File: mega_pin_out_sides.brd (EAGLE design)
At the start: 100 x 85 mm, 101 parts, among them T1 2N2222, T10 2N2222, T11 2N2222, T12 2N2222, T13 2N2222, T14 2N2222, T15 2N2222, T16 2N2222, T17 2N2222, T18 2N2222, T2 2N2222, T3 2N2222, T4 2N2222, T5 2N2222, T6 2N2222, T7 2N2222, T8 2N2222, T9 2N2222

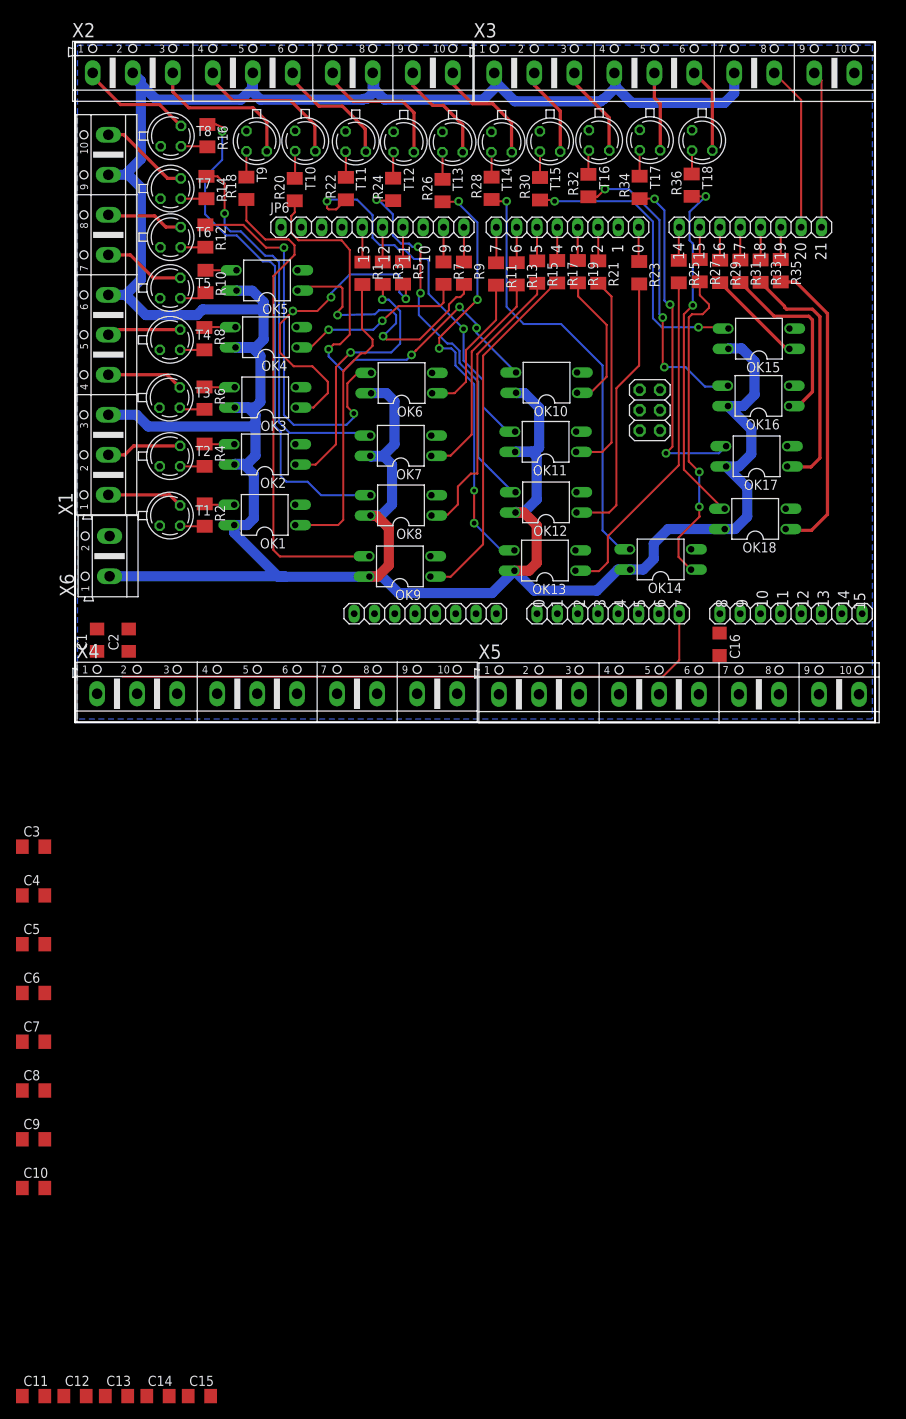
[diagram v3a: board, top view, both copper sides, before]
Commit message: [SIDES] Fix major issue where GND was common
- Fix a major bug in the design where the Vext GND and Arduino GND were common. They have been isolated correctly.
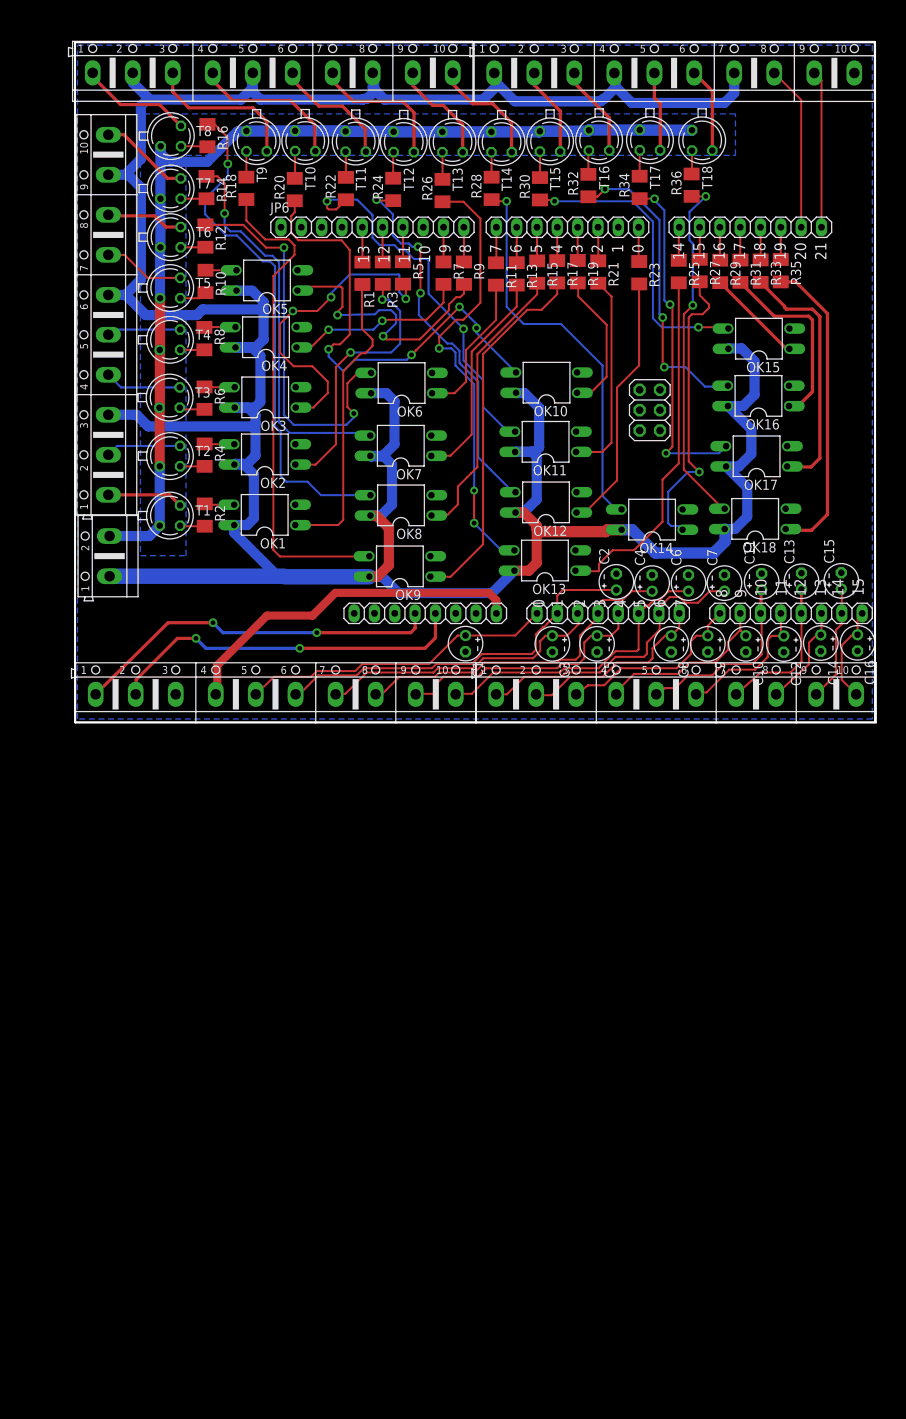
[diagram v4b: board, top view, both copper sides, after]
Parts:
- C1, C10, C11, C12, C13, C14, C15, C16, C2, C3, C4, C5, C6, C7, C8, C9: device resistor:C1206 -> adafruit:E2-4
- moved C11 136.6 mm to (85.8, 17.6), turned to 90 degrees
- moved C13 133.1 mm to (90.8, 17.6), turned to 90 degrees
- moved C15 129.7 mm to (95.8, 17.7), turned to 90 degrees
- moved C12 129.2 mm to (88.6, 9.78), turned to 270 degrees
- moved C14 125.4 mm to (93.2, 9.91), turned to 270 degrees
- moved C10 112.0 mm to (83.8, 9.80), turned to 270 degrees
- moved C9 104.6 mm to (79.1, 9.80), turned to 270 degrees
- moved C7 103.7 mm to (81.2, 17.4), turned to 90 degrees
- moved C8 97.3 mm to (74.5, 9.80), turned to 270 degrees
- moved C6 96.6 mm to (76.7, 17.4), turned to 90 degrees
- moved C4 86.6 mm to (72.1, 17.4), turned to 90 degrees
- moved C5 79.8 mm to (65.3, 9.80), turned to 270 degrees
- moved C3 69.6 mm to (59.7, 9.80), turned to 270 degrees
- moved C2 61.4 mm to (67.7, 17.6)
- moved C1 46.1 mm to (48.8, 9.83), turned to 270 degrees
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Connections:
- new net GNDEXT: T1.1, T10.1, T11.1, T12.1, T13.1, T14.1, T15.1, T16.1, T17.1, T18.1, T2.1, T3.1, T4.1, T5.1, T6.1, T7.1, T8.1, T9.1, X6.2
- net A0: now also ADCL.1, C1.+; no longer ADCL.8
- net A1: now also ADCL.2, C2.+; no longer ADCL.7
- net A10: now also ADCH.3, C11.+; no longer ADCH.6, C11.1
- net A11: now also ADCH.4, C12.+; no longer ADCH.5, C12.1
- net A12: now also ADCH.5, C13.+; no longer ADCH.4, C13.1
- net A13: now also ADCH.6, C14.+; no longer ADCH.3, C14.1
- net A14: now also ADCH.7, C15.+; no longer ADCH.2, C15.1
- net A15: now also ADCH.8, C16.+; no longer ADCH.1, C16.1
- net A2: now also ADCL.3, C3.+; no longer ADCL.6
- net A3: now also ADCL.4, C4.+; no longer ADCL.5
- net A4: now also ADCL.5, C5.+; no longer ADCL.4
- net A5: now also ADCL.6, C6.+; no longer ADCL.3
- net A6: now also ADCL.7, C7.+; no longer ADCL.2
- net A7: now also ADCL.8, C8.+; no longer ADCL.1
- net A8: now also ADCH.1, C9.+; no longer ADCH.8
- net A9: now also ADCH.2, C10.+; no longer ADCH.7
- net GND: now also C1.-, C10.-, C11.-, C12.-, C13.-, C14.-, C15.-, C16.-, C2.-, C3.-, C4.-, C5.-, C6.-, C7.-, C8.-, C9.-; no longer C1.2, C10.2, C11.2, C12.2, C13.2, C14.2, C15.2, C16.2, C2.2, C3.2, C4.2, C5.2, C6.2, C7.2, C8.2, C9.2, T1.1, T10.1, T11.1, T12.1, T13.1, T14.1, T15.1, T16.1, T17.1, T18.1, T2.1, T3.1, T4.1, T5.1, T6.1, T7.1, T8.1, T9.1
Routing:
- net GNDEXT: track 0.00 -> 124.4 mm
- net A1: track 0.00 -> 48.0 mm
- net 3V3: track 0.00 -> 46.2 mm, vias 0 -> 2
- net 5V: track 0.00 -> 45.5 mm, vias 0 -> 2
- net VIN: track 0.00 -> 44.4 mm
- net A3: track 0.00 -> 42.4 mm
- net A6: track 0.00 -> 37.1 mm
- net A5: track 0.00 -> 37.1 mm
- net A0: track 76.3 -> 39.3 mm
- net A2: track 0.00 -> 36.1 mm
- net A4: track 0.00 -> 32.3 mm
- net A10: track 0.00 -> 26.2 mm
- net A7: track 0.00 -> 23.9 mm
- net A8: track 0.00 -> 23.7 mm
- net A9: track 0.00 -> 22.6 mm
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- added copper zone on layer 16, net N$3

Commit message: [SIDES] Fix DRC Errors
- Fixed all DRC Errors which were related to silk screens mainly.
- Re routed some pins for a better path.
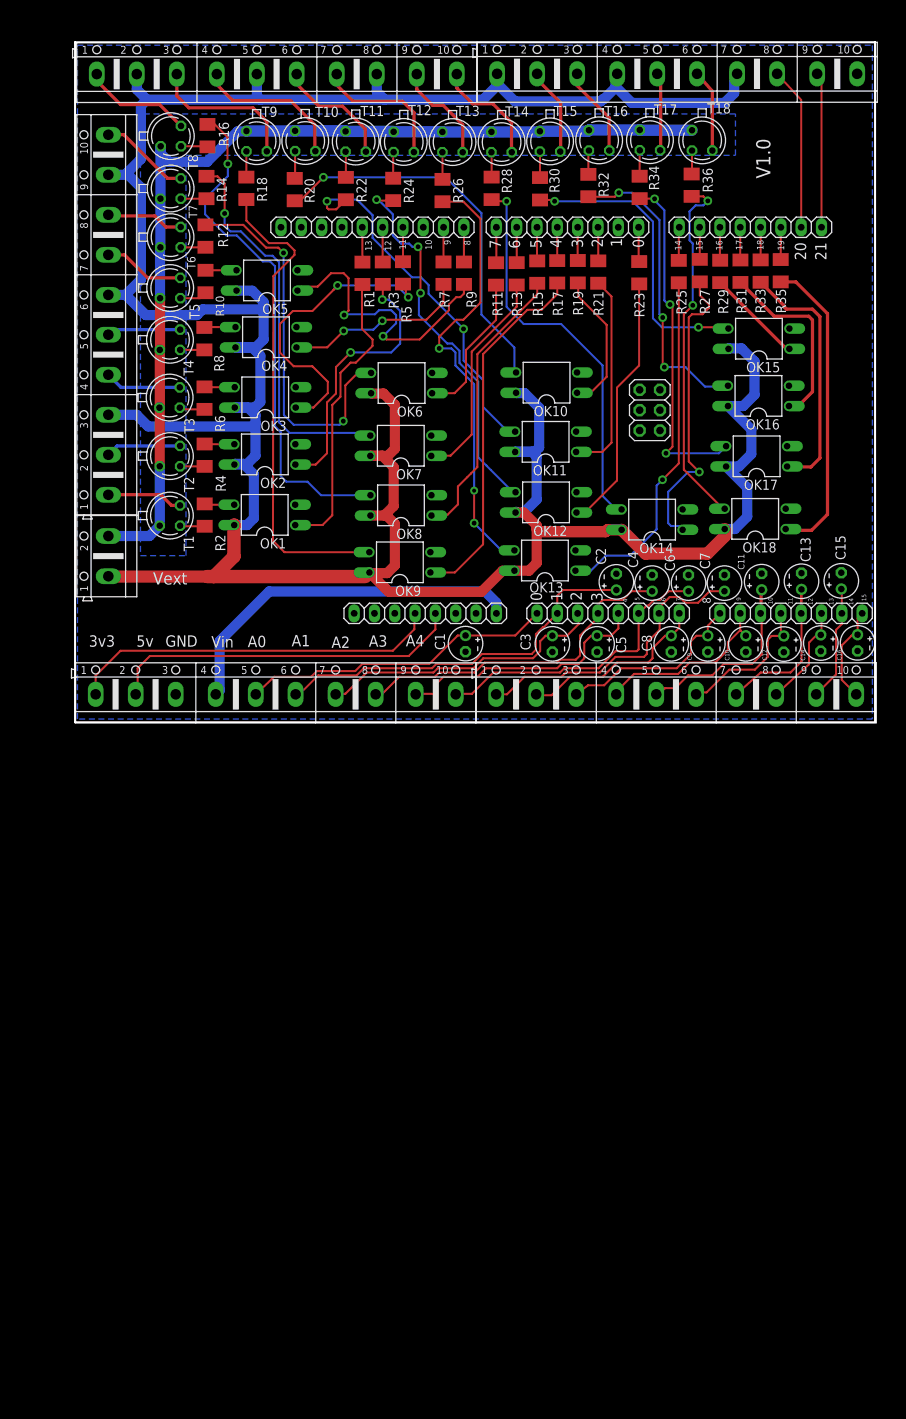
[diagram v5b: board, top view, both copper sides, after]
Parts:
- moved X2 0.53 mm to (25.2, 81.0)
- moved OK9 0.51 mm to (40.6, 20.0)
- moved X3 0.37 mm to (75.3, 81.1)
- moved X6 0.15 mm to (4.16, 20.8)
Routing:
- net N$36: track 58.9 -> 48.1 mm, vias 4 -> 1
- net VEXT: track 407.9 -> 403.4 mm
- net N$8: track 40.4 -> 37.8 mm, vias 3 -> 2
- net N$14: track 34.8 -> 36.9 mm
- net N$39: track 47.8 -> 46.0 mm
- net N$24: track 49.7 -> 48.0 mm
- net VIN: track 44.4 -> 45.9 mm
- net N$33: track 61.5 -> 60.2 mm
- net N$1: track 38.1 -> 37.0 mm
- net 5V: track 45.5 -> 44.6 mm, vias 2 -> 0
- net N$57: track 44.5 -> 45.1 mm
- net N$47: track 44.7 -> 44.3 mm, vias 0 -> 1
- net 3V3: track 46.2 -> 46.6 mm, vias 2 -> 0
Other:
- board text added: "3v3"
- board text added: "5v"
- board text added: "A0"
- board text added: "A1"
- board text added: "A2"
- board text added: "A3"
- board text added: "A4"
- board text added: "GND"
- board text added: "V1.0"
- board text added: "Vext"
- board text added: "Vin"

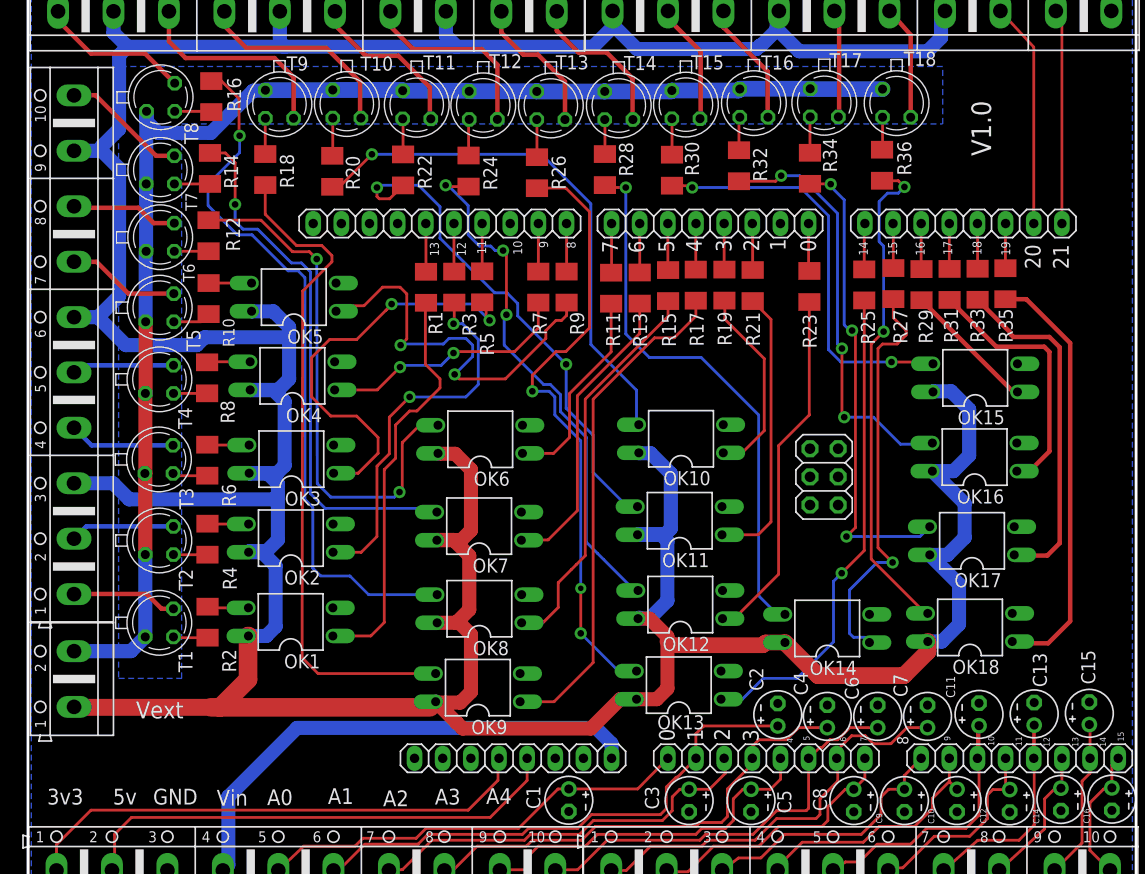
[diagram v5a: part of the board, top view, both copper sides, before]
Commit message: [SIDES] Added header jumper pins for Flashing
- During Flashing or Reset Pin 13, 9 & 0 flashes several times and this will trigger the relays. A header jumper to be removed during flashing and after start up they are back again in place.
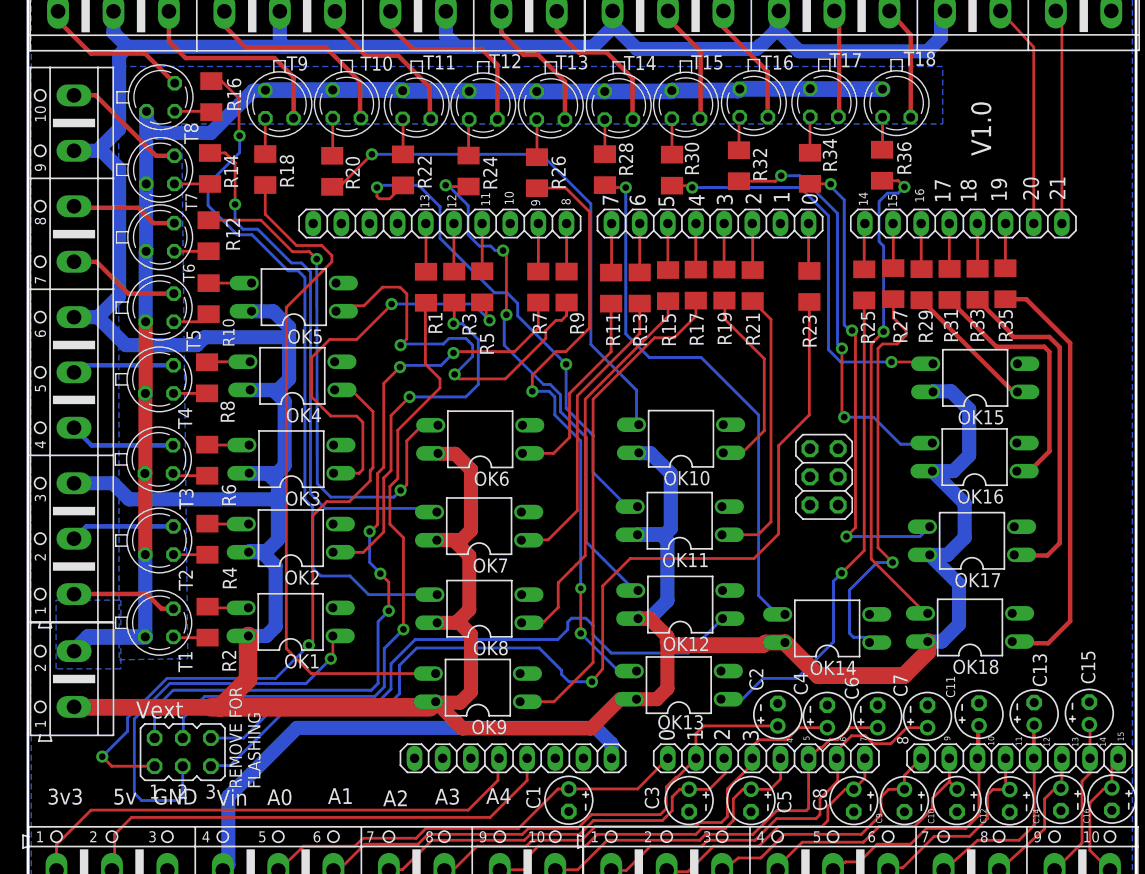
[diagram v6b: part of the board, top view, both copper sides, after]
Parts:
- added JP1: (no value), jumper:JP3Q
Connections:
- new net N$10: JP1.6, OK12.1
- new net N$11: JP1.1, OK4.1
- new net N$9: JP1.3, OK1.1
- net GND: now also X3.10
- net N$1: now also JP1.4; no longer OK1.1
- net N$19: now also JP1.2; no longer OK4.1
- net N$44: now also JP1.5; no longer OK12.1
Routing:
- net N$44: track 32.4 -> 90.7 mm, vias 0 -> 1
- net N$11: track 0.00 -> 57.6 mm, vias 0 -> 2
- net N$10: track 0.00 -> 55.5 mm
- net N$19: track 23.0 -> 70.8 mm, vias 2 -> 5
- net N$9: track 0.00 -> 36.3 mm, vias 0 -> 1
- net N$1: track 37.0 -> 59.5 mm, vias 0 -> 1
- net N$33: track 60.2 -> 61.8 mm
- net N$8: track 37.8 -> 36.8 mm
- added copper zone on layer 16, net N$62
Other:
- board text added: "REMOVE FOR FLASHING"

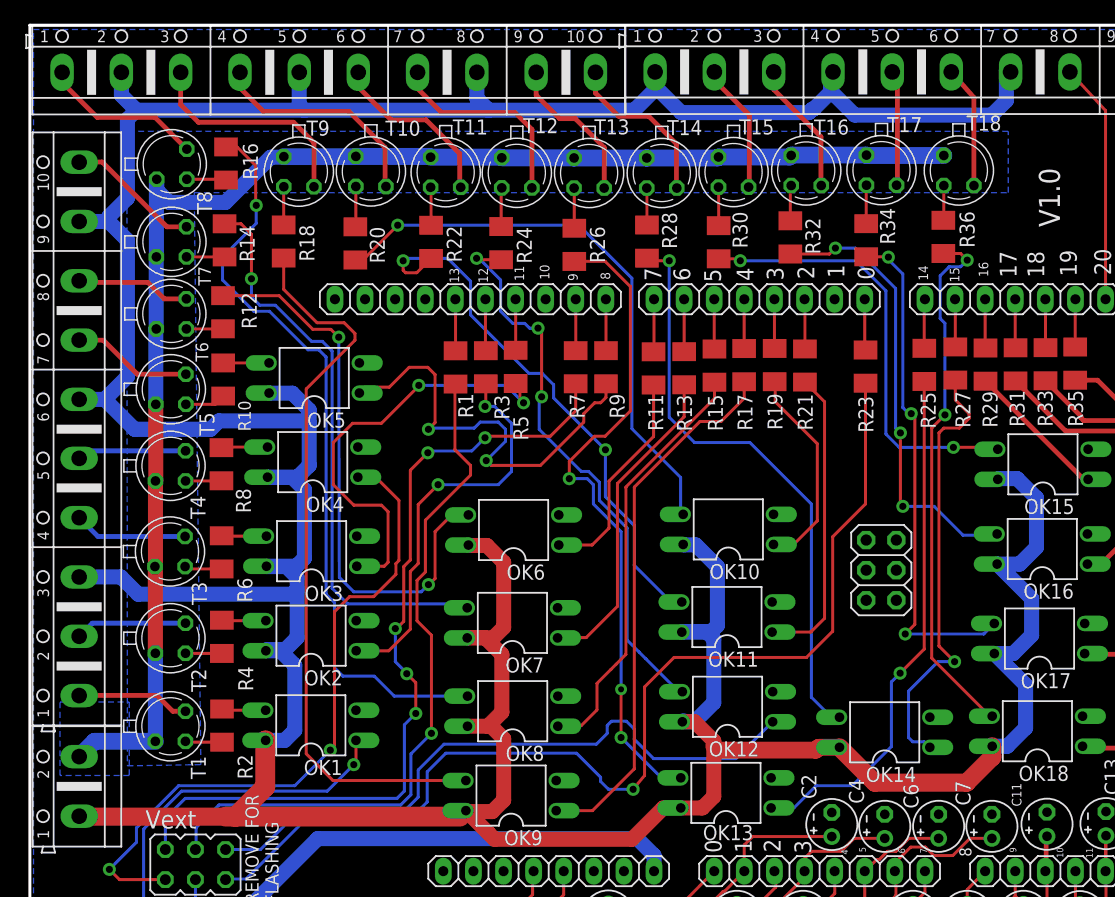
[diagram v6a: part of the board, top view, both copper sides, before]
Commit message: [SIDES] Placed Vext & Gext on a separate layer
External voltage is routed on the top layer instead to be isolated from the ground plane.
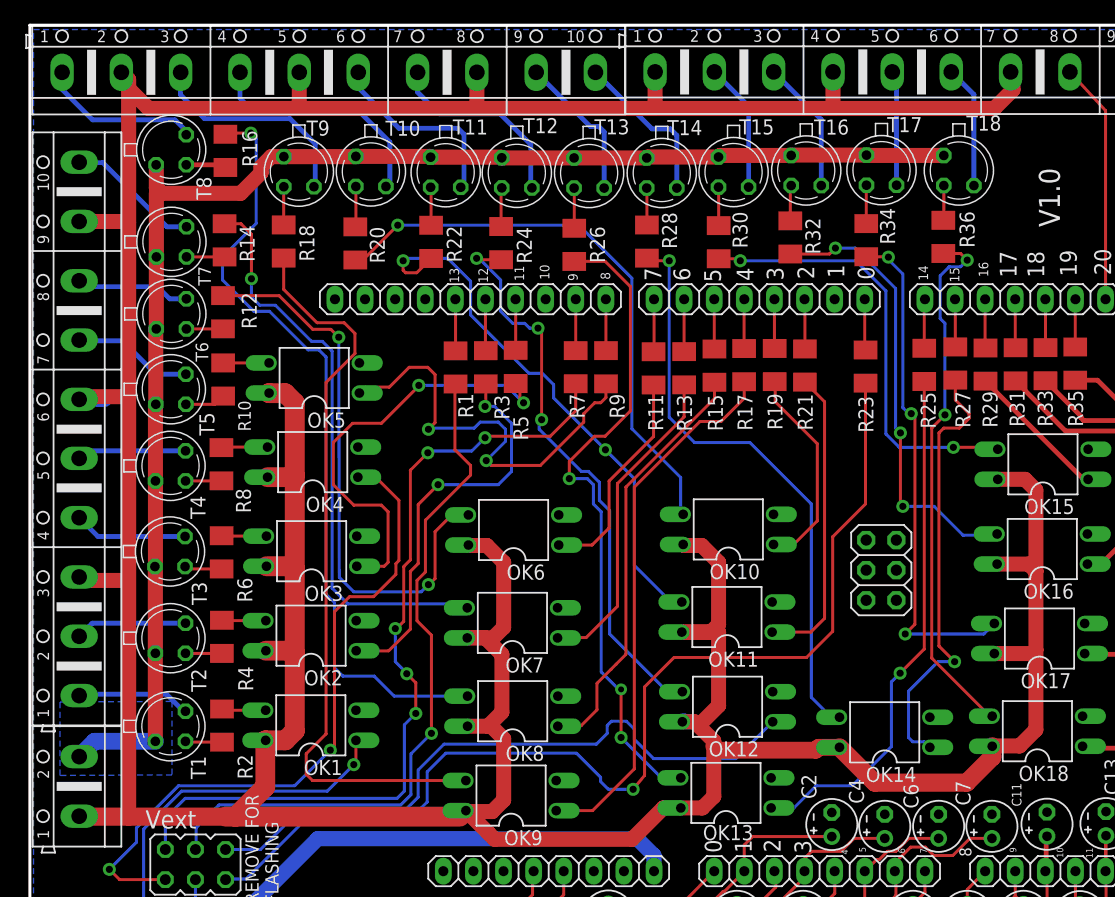
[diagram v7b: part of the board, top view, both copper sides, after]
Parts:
- moved T8 1.22 mm to (11.9, 74.5)
- moved R16 1.07 mm to (16.5, 74.4)
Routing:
- net N$30: track 64.2 -> 66.1 mm
- net 2BJT: track 15.0 -> 16.4 mm
- net 3BJT: track 19.0 -> 20.3 mm
- net N$33: track 61.8 -> 62.8 mm
- net N$45: track 47.7 -> 48.6 mm
- net 0BJT: track 17.4 -> 16.8 mm
- net 15BJT: track 14.1 -> 13.5 mm
- net VEXT: track 403.4 -> 402.8 mm
- removed copper zone on layer 16, net N$3
